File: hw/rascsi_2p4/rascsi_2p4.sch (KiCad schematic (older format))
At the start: 63 parts, among them J1 Raspberry_Pi_2_3, J2 DNP, J4 I2C Pinout, J5 DNP, J6 CONNFLY DB-25, J7 DNP, U1 SN74LS641-1DW, U2 SN74LS641-1DW, U3 SN74LS641-1DW, U4 SN74LS641-1DW, U5 UCC5606PWPTR, U6 UCC5606PWPTR, X1 Mac, X3 Mac, X7 Pi, X8 Pi

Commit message: added jlcpcb part number of scsi terminator
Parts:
- U5, U6: LCSC (none) -> C2649373; Manufacturer_Name (none) -> Texas Instruments
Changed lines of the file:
@@
 F 2 "Package_SO:TSSOP-24_6.1x7.8mm_P0.65mm" H 7500 400 50  0001 C CNN
 F 3 "http://www.ti.com/general/docs/suppproductinfo.tsp?distId=26&gotoUrl=http%3A%2F%2Fwww.ti.com%2Flitv%2Fslus347a" H 7800 950 50  0001 C CNN
+F 4 "C2649373" H 7500 1750 50  0001 C CNN "LCSC"
+F 5 "Texas Instruments" H 7500 1750 50  0001 C CNN "Manufacturer_Name"
 	1    7500 1750
 	1    0    0    -1
@@
 F 2 "Package_SO:TSSOP-24_6.1x7.8mm_P0.65mm" H 9300 400 50  0001 C CNN
 F 3 "http://www.ti.com/general/docs/suppproductinfo.tsp?distId=26&gotoUrl=http%3A%2F%2Fwww.ti.com%2Flitv%2Fslus347a" H 9600 950 50  0001 C CNN
+F 4 "C2649373" H 9300 1750 50  0001 C CNN "LCSC"
+F 5 "Texas Instruments" H 9300 1750 50  0001 C CNN "Manufacturer_Name"
 	1    9300 1750
 	1    0    0    -1

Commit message: set BOM fields to DNP
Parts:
- JP3: Description (none) -> DNP; LCSC (none) -> DNP; Manufacturer_Name (none) -> DNP; Manufacturer_Part_Number (none) -> DNP
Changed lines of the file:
@@
 F 1 "PULLUP Power" H 950 7563 50  0000 C CNN
 F 2 "Jumper:SolderJumper-3_P1.3mm_Bridged12_RoundedPad1.0x1.5mm" H 950 7450 50  0001 C CNN
-F 3 "~" H 950 7450 50  0001 C CNN
+F 3 "DNP" H 950 7450 50  0001 C CNN
+F 4 "DNP" H 950 7450 50  0001 C CNN "Description"
+F 5 "DNP" H 950 7450 50  0001 C CNN "LCSC"
+F 6 "DNP" H 950 7450 50  0001 C CNN "Manufacturer_Name"
+F 7 "DNP" H 950 7450 50  0001 C CNN "Manufacturer_Part_Number"
 	1    950  7450
 	1    0    0    -1

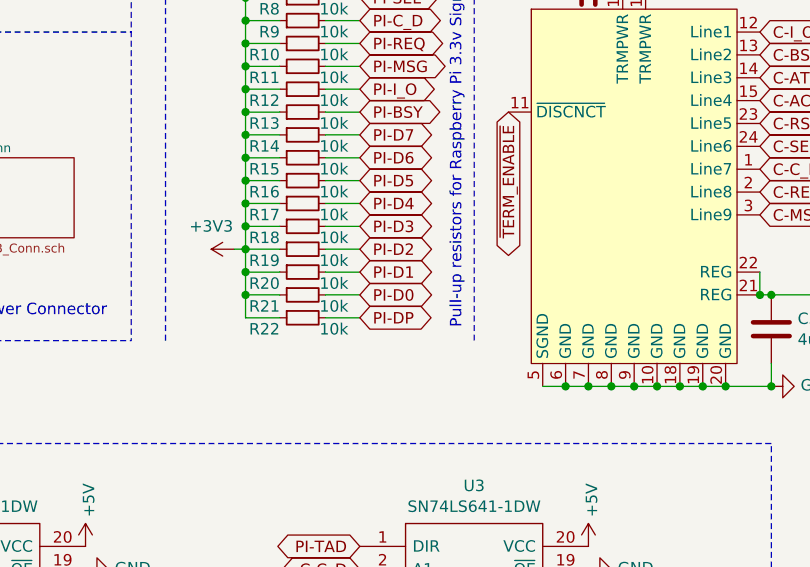
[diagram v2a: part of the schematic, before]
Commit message: swapped R18 and R22 slightly moved R14 to R18
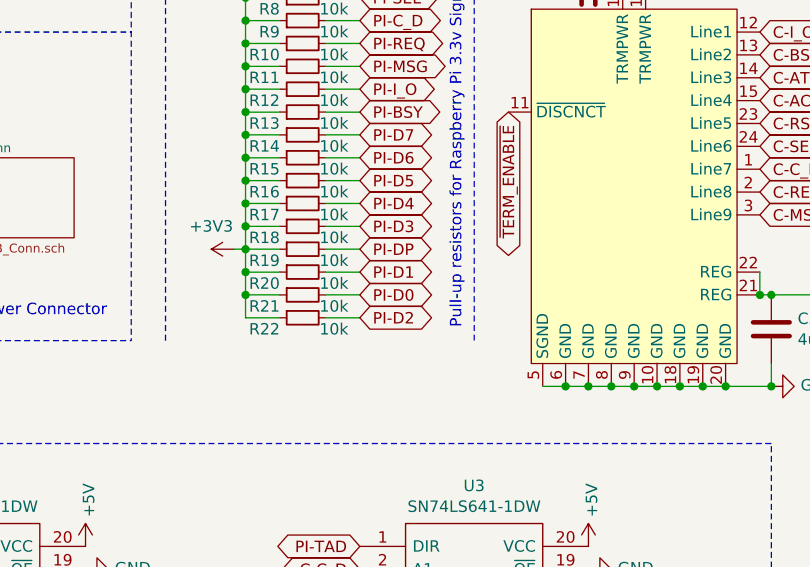
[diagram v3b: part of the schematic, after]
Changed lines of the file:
@@
 Text GLabel 6300 2150 2    50   BiDi ~ 0
 PI-D1
-Text GLabel 6300 2050 2    50   BiDi ~ 0
+Text GLabel 6300 2350 2    50   BiDi ~ 0
 PI-D2
 Text GLabel 6300 1950 2    50   BiDi ~ 0
@@
 Text GLabel 6300 950  2    50   BiDi ~ 0
 PI-SEL
-Text GLabel 6300 2350 2    50   BiDi ~ 0
+Text GLabel 6300 2050 2    50   BiDi ~ 0
 PI-DP
 Text GLabel 1200 1000 1    50   BiDi ~ 0

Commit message: made 25pin and USB conn placeable by JLCPCB
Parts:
- J6: footprint SamacSys_Parts:L717SDB25PA4CH4F -> SamacSys_Parts:L717SDB25PA4CH4F_JLCPCB_hand_mount
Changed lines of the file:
@@
 F 0 "J6" V 9019 3000 50  0000 C CNN
 F 1 "CONNFLY DB-25" V 9110 3000 50  0000 C CNN
-F 2 "SamacSys_Parts:L717SDB25PA4CH4F" H 10850 3300 50  0001 L CNN
+F 2 "SamacSys_Parts:L717SDB25PA4CH4F_JLCPCB_hand_mount" H 10850 3300 50  0001 L CNN
 F 3 "https://datasheet.lcsc.com/szlcsc/1811081022_CONNFLY-Elec-DS1037-25FNAKT74-0CC_C77838.pdf" H 10850 3200 50  0001 L CNN
 F 4 "D-Sub Receptacle,Female Socket 25 2 1.5A(Contact) Through Hole D-Sub Connectors RoHS" H 10850 3100 50  0001 L CNN "Description"

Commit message: changed /TERM_ENABLE to TERM_ENABLE so that a plugged jumper enables termination
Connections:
- net labels added: TERM_ENABLE
- net labels removed: ~TERM_ENABLE
- wire segments 158 -> 156
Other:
- moved on the sheet: R24
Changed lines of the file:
@@
 L power:GND #PWR014
 U 1 1 6072B62D
-P 3000 1000
-F 0 "#PWR014" H 3000 750 50  0001 C CNN
-F 1 "GND" H 2850 950 50  0000 C CNN
-F 2 "" H 3000 1000 50  0001 C CNN
-F 3 "" H 3000 1000 50  0001 C CNN
-	1    3000 1000
+P 3050 900
+F 0 "#PWR014" H 3050 650 50  0001 C CNN
+F 1 "GND" H 3050 750 50  0000 C CNN
+F 2 "" H 3050 900 50  0001 C CNN
+F 3 "" H 3050 900 50  0001 C CNN
+	1    3050 900
 	-1   0    0    1
 $EndComp
-Wire Wire Line
-	3250 1000 3000 1000
-Text Notes 2950 650  0    50   ~ 0
-Termination Enable Jumper
 Wire Notes Line
 	2900 550  5300 550
@@
 	1200 1400 1200 1450
 Text GLabel 6950 1450 3    50   BiDi ~ 0
-~TERM_ENABLE
+TERM_ENABLE
 $Comp
 L amiga:UCC5606PWPTR U6
@@
 	9250 900  9350 900
 Text GLabel 8750 1450 3    50   BiDi ~ 0
-~TERM_ENABLE
+TERM_ENABLE
 Text Notes 8900 650  2    50   ~ 0
 Active SCSI Termination
@@
 Wire Wire Line
 	1400 1400 1400 1100
-Text GLabel 3900 1000 2    50   BiDi ~ 0
-~TERM_ENABLE
 $Comp
 L Device:R_Small R24
 U 1 1 63241307
-P 4050 750
-F 0 "R24" V 4150 700 50  0000 L CNN
-F 1 "10k" V 4150 550 50  0000 L CNN
-F 2 "Resistor_SMD:R_0402_1005Metric" H 4050 750 50  0001 C CNN
-F 3 "https://datasheet.lcsc.com/szlcsc/1809301717_UNI-ROYAL-Uniroyal-Elec-0402WGF1002TCE_C25744.pdf" H 4050 750 50  0001 C CNN
-F 4 "C25744" H 4050 750 50  0001 C CNN "LCSC"
-F 5 "10kΩ ±1% 1/16W ±100ppm/℃ 0402 Chip Resistor" H 4050 750 50  0001 C CNN "Description"
-F 6 "UNI-ROYAL(Uniroyal Elec)" H 4050 750 50  0001 C CNN "Manufacturer_Name"
-F 7 "0402WGF1002TCE" H 4050 750 50  0001 C CNN "Manufacturer_Part_Number"
-	1    4050 750
+P 3250 900
+F 0 "R24" V 3150 800 50  0000 L CNN
+F 1 "10k" V 3050 800 50  0000 L CNN
+F 2 "Resistor_SMD:R_0402_1005Metric" H 3250 900 50  0001 C CNN
+F 3 "https://datasheet.lcsc.com/szlcsc/1809301717_UNI-ROYAL-Uniroyal-Elec-0402WGF1002TCE_C25744.pdf" H 3250 900 50  0001 C CNN
+F 4 "C25744" H 3250 900 50  0001 C CNN "LCSC"
+F 5 "10kΩ ±1% 1/16W ±100ppm/℃ 0402 Chip Resistor" H 3250 900 50  0001 C CNN "Description"
+F 6 "UNI-ROYAL(Uniroyal Elec)" H 3250 900 50  0001 C CNN "Manufacturer_Name"
+F 7 "0402WGF1002TCE" H 3250 900 50  0001 C CNN "Manufacturer_Part_Number"
+	1    3250 900
 	0    -1   1    0
 $EndComp
-$Comp
-L power:+5V #PWR0112
-U 1 1 63255B5E
-P 4200 750
-F 0 "#PWR0112" H 4200 600 50  0001 C CNN
-F 1 "+5V" H 4200 900 50  0000 C CNN
-F 2 "" H 4200 750 50  0001 C CNN
-F 3 "" H 4200 750 50  0001 C CNN
-	1    4200 750
-	0    1    1    0
-$EndComp
-Text GLabel 650  1200 1    50   BiDi ~ 0
-~TERM_ENABLE
+Text GLabel 800  1000 1    50   BiDi ~ 0
+TERM_ENABLE
 $Comp
 L Device:R_Small R23
@@
 	1600 1700 1950 1700
 Connection ~ 1950 1700
-$Comp
-L power:+5V #PWR0113
-U 1 1 633F91EE
-P 800 1000
-F 0 "#PWR0113" H 800 850 50  0001 C CNN
-F 1 "+5V" V 815 1128 50  0000 L CNN
-F 2 "" H 800 1000 50  0001 C CNN
-F 3 "" H 800 1000 50  0001 C CNN
-	1    800  1000
-	1    0    0    -1
-$EndComp
 Wire Wire Line
 	800  1300 800  1450
@@
 	1200 1700 1600 1700
 Wire Wire Line
-	650  1200 650  1700
-Wire Wire Line
-	650  1700 800  1700
-Wire Wire Line
 	1950 1700 2300 1700
-Wire Wire Line
-	3800 1000 3900 1000
-Wire Wire Line
-	4150 750  4200 750
-Wire Wire Line
-	3800 750  3950 750
 Text GLabel 3750 1600 0    50   BiDi ~ 0
 TERMPOW_UNFUSED
@@
 L Jumper:Jumper_2_Open JP2
 U 1 1 614F73E7
-P 3450 1000
-F 0 "JP2" H 3450 1235 50  0000 C CNN
-F 1 "Jumper_2_Open" H 3450 1144 50  0000 C CNN
-F 2 "Connector_PinHeader_2.54mm:PinHeader_1x02_P2.54mm_Horizontal" H 3450 1000 50  0001 C CNN
-F 3 "~" H 3450 1000 50  0001 C CNN
-	1    3450 1000
-	1    0    0    -1
-$EndComp
-Wire Wire Line
-	3800 750  3800 1000
-Wire Wire Line
-	3650 1000 3800 1000
-Connection ~ 3800 1000
+P 3650 900
+F 0 "JP2" H 3650 1050 50  0000 C CNN
+F 1 "Jumper_2_Open" H 4050 1050 50  0000 C CNN
+F 2 "Connector_PinHeader_2.54mm:PinHeader_1x02_P2.54mm_Horizontal" H 3650 900 50  0001 C CNN
+F 3 "~" H 3650 900 50  0001 C CNN
+	1    3650 900
+	1    0    0    -1
+$EndComp
 Text GLabel 5100 4250 2    50   BiDi ~ 0
 PULLUP_OC
@@
 Wire Notes Line
 	2900 1100 5300 1100
+Wire Wire Line
+	3050 900  3150 900
+$Comp
+L power:+5V #PWR0112
+U 1 1 63255B5E
+P 3850 900
+F 0 "#PWR0112" H 3850 750 50  0001 C CNN
+F 1 "+5V" H 3850 1050 50  0000 C CNN
+F 2 "" H 3850 900 50  0001 C CNN
+F 3 "" H 3850 900 50  0001 C CNN
+	1    3850 900
+	0    1    1    0
+$EndComp
+Text GLabel 4200 1000 2    50   BiDi ~ 0
+TERM_ENABLE
+Text Notes 3450 650  0    50   ~ 0
+Termination Enable Jumper
+Wire Wire Line
+	3350 900  3400 900
+Wire Wire Line
+	3400 1000 4200 1000
+Wire Wire Line
+	3400 1000 3400 900
+Connection ~ 3400 900
+Wire Wire Line
+	3400 900  3450 900
+Wire Wire Line
+	800  1700 1200 1700
+Connection ~ 1200 1700
 $EndSCHEMATC

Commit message: fixed wiring of U3 and U4 fixed priority of term enable
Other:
- note added: "Here the Pi is connected to Port A"
- note added: "Here the Pi is connected to Port B"
- note added: "RaSCSI - 68kmlat Edition - with active termination"
- note removed: "RaSCSI - 68kmla Edition - with active termination"
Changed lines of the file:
@@
 	2700 550  2700 2450
 Text Notes 6750 7760 0    87   ~ 17
-RaSCSI - 68kmla Edition - with active termination
+RaSCSI - 68kmlat Edition - with active termination
 Text Notes 9900 7890 0    79   ~ 16
 2.4
@@
 $EndComp
 $Comp
-L power:GND #PWR0123
-U 1 1 611ED586
-P 7300 3450
-F 0 "#PWR0123" H 7300 3200 50  0001 C CNN
-F 1 "GND" V 7305 3322 50  0000 R CNN
-F 2 "" H 7300 3450 50  0001 C CNN
-F 3 "" H 7300 3450 50  0001 C CNN
-	1    7300 3450
-	0    -1   -1   0
-$EndComp
-$Comp
 L power:GND #PWR0124
 U 1 1 611ED58C
@@
 	1    7300 4700
 	1    0    0    -1
-$EndComp
-$Comp
-L power:GND #PWR0126
-U 1 1 611ED5A5
-P 7300 4800
-F 0 "#PWR0126" H 7300 4550 50  0001 C CNN
-F 1 "GND" V 7305 4672 50  0000 R CNN
-F 2 "" H 7300 4800 50  0001 C CNN
-F 3 "" H 7300 4800 50  0001 C CNN
-	1    7300 4800
-	0    -1   -1   0
 $EndComp
 $Comp
@@
 Text GLabel 5100 5400 2    50   BiDi ~ 0
 PULLUP_OC
+Text GLabel 7300 3550 2    50   BiDi ~ 0
+C-BSY
+Text GLabel 7300 4050 2    50   BiDi ~ 0
+C-MSG
+Text GLabel 7300 4250 2    50   BiDi ~ 0
+C-C_D
+Text GLabel 7300 3650 2    50   BiDi ~ 0
+C-I_O
+Text GLabel 7300 4150 2    50   BiDi ~ 0
+C-REQ
+Text GLabel 7300 3850 2    50   BiDi ~ 0
+PULLUP_OC
+Text GLabel 7300 3750 2    50   BiDi ~ 0
+PULLUP_OC
+Text GLabel 7300 3950 2    50   BiDi ~ 0
+PULLUP_OC
+Text GLabel 7300 4900 2    50   BiDi ~ 0
+PULLUP_OC
+Text GLabel 6300 5500 0    50   BiDi ~ 0
+PI-ATN
+Text GLabel 6300 5300 0    50   BiDi ~ 0
+PI-RST
+Text GLabel 6300 5200 0    50   BiDi ~ 0
+PI-SEL
+Text GLabel 6300 5400 0    50   BiDi ~ 0
+PI-ACK
+Text GLabel 6300 4050 0    50   BiDi ~ 0
+PI-REQ
 Text GLabel 6300 4150 0    50   BiDi ~ 0
-C-BSY
+PI-C_D
+Text GLabel 6300 3950 0    50   BiDi ~ 0
+PI-MSG
+Text GLabel 6300 3450 0    50   BiDi ~ 0
+PI-BSY
+Text GLabel 6300 3550 0    50   BiDi ~ 0
+PI-I_O
+Text GLabel 6300 3750 0    50   BiDi ~ 0
+PULLUP_OC
 Text GLabel 6300 3650 0    50   BiDi ~ 0
-C-MSG
-Text GLabel 6300 3450 0    50   BiDi ~ 0
-C-C_D
-Text GLabel 6300 4050 0    50   BiDi ~ 0
-C-I_O
-Text GLabel 6300 3550 0    50   BiDi ~ 0
-C-REQ
+PULLUP_OC
+Text GLabel 6300 3850 0    50   BiDi ~ 0
+PULLUP_OC
+Text GLabel 6300 5100 0    50   BiDi ~ 0
+PULLUP_OC
+Text GLabel 6300 5000 0    50   BiDi ~ 0
+PULLUP_OC
+Text GLabel 6300 4900 0    50   BiDi ~ 0
+PULLUP_OC
 Text GLabel 6300 4800 0    50   BiDi ~ 0
-C-ATN
-Text GLabel 6300 4900 0    50   BiDi ~ 0
-C-ACK
-Text GLabel 6300 5000 0    50   BiDi ~ 0
-C-RST
-Text GLabel 6300 5100 0    50   BiDi ~ 0
-C-SEL
-Text GLabel 6300 3850 0    50   BiDi ~ 0
-PULLUP_OC
-Text GLabel 6300 3950 0    50   BiDi ~ 0
-PULLUP_OC
-Text GLabel 6300 3750 0    50   BiDi ~ 0
-PULLUP_OC
-Text GLabel 6300 5200 0    50   BiDi ~ 0
-PULLUP_OC
-Text GLabel 6300 5300 0    50   BiDi ~ 0
-PULLUP_OC
-Text GLabel 6300 5400 0    50   BiDi ~ 0
-PULLUP_OC
-Text GLabel 6300 5500 0    50   BiDi ~ 0
-PULLUP_OC
-Text GLabel 7300 4900 2    50   BiDi ~ 0
-PI-ATN
-Text GLabel 7300 5100 2    50   BiDi ~ 0
-PI-RST
-Text GLabel 7300 5200 2    50   BiDi ~ 0
-PI-SEL
-Text GLabel 7300 5000 2    50   BiDi ~ 0
-PI-ACK
-Text GLabel 7300 3650 2    50   BiDi ~ 0
-PI-REQ
-Text GLabel 7300 3550 2    50   BiDi ~ 0
-PI-C_D
-Text GLabel 7300 3750 2    50   BiDi ~ 0
-PI-MSG
-Text GLabel 7300 4250 2    50   BiDi ~ 0
-PI-BSY
-Text GLabel 7300 4150 2    50   BiDi ~ 0
-PI-I_O
-Text GLabel 7300 3950 2    50   BiDi ~ 0
-PULLUP_OC
-Text GLabel 7300 4050 2    50   BiDi ~ 0
-PULLUP_OC
-Text GLabel 7300 3850 2    50   BiDi ~ 0
-PULLUP_OC
-Text GLabel 7300 5300 2    50   BiDi ~ 0
-PULLUP_OC
-Text GLabel 7300 5400 2    50   BiDi ~ 0
-PULLUP_OC
-Text GLabel 7300 5500 2    50   BiDi ~ 0
-PULLUP_OC
-Text GLabel 7300 5600 2    50   BiDi ~ 0
 PULLUP_OC
 Wire Wire Line
@@
 	800  1700 1200 1700
 Connection ~ 1200 1700
+Text GLabel 7300 5000 2    50   BiDi ~ 0
+PULLUP_OC
+Text GLabel 7300 5100 2    50   BiDi ~ 0
+PULLUP_OC
+Text GLabel 7300 5200 2    50   BiDi ~ 0
+PULLUP_OC
+Text GLabel 7300 5300 2    50   BiDi ~ 0
+C-SEL
+Text GLabel 7300 5400 2    50   BiDi ~ 0
+C-RST
+Text GLabel 7300 5500 2    50   BiDi ~ 0
+C-ACK
+Text GLabel 7300 5600 2    50   BiDi ~ 0
+C-ATN
+$Comp
+L power:GND #PWR0126
+U 1 1 611ED5A5
+P 7300 4800
+F 0 "#PWR0126" H 7300 4550 50  0001 C CNN
+F 1 "GND" V 7305 4672 50  0000 R CNN
+F 2 "" H 7300 4800 50  0001 C CNN
+F 3 "" H 7300 4800 50  0001 C CNN
+	1    7300 4800
+	0    -1   -1   0
+$EndComp
+$Comp
+L power:GND #PWR0123
+U 1 1 611ED586
+P 7300 3450
+F 0 "#PWR0123" H 7300 3200 50  0001 C CNN
+F 1 "GND" V 7305 3322 50  0000 R CNN
+F 2 "" H 7300 3450 50  0001 C CNN
+F 3 "" H 7300 3450 50  0001 C CNN
+	1    7300 3450
+	0    -1   -1   0
+$EndComp
+Text Notes 6050 3050 0    59   Italic 0
+Here the Pi is connected to Port A
+Text Notes 3800 3050 0    59   Italic 0
+Here the Pi is connected to Port B
 $EndSCHEMATC
